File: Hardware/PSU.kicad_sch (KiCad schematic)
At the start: 20 parts, among them SW1 Power_Hard, SW2 Power_Soft, U4 TLV74115_SOT23-5, U5 TLV74133_SOT23-5

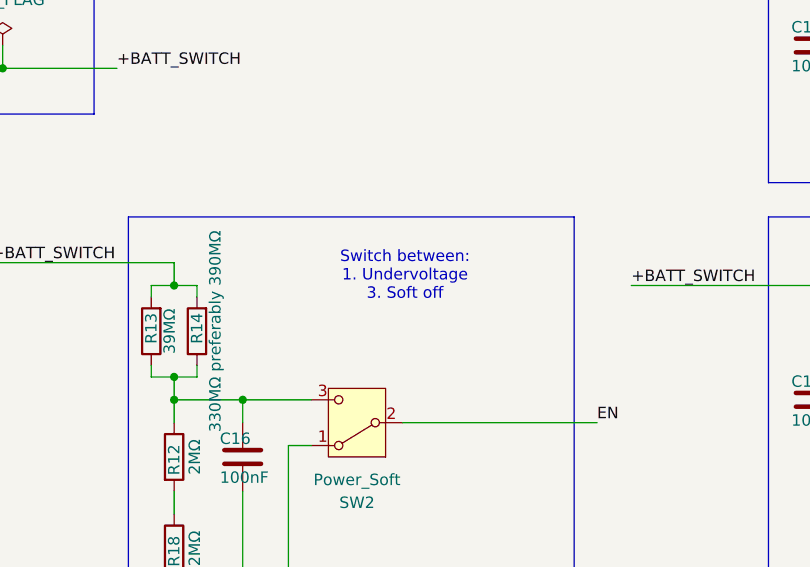
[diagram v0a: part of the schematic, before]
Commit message: Changed text PSU EN switch to match circuit
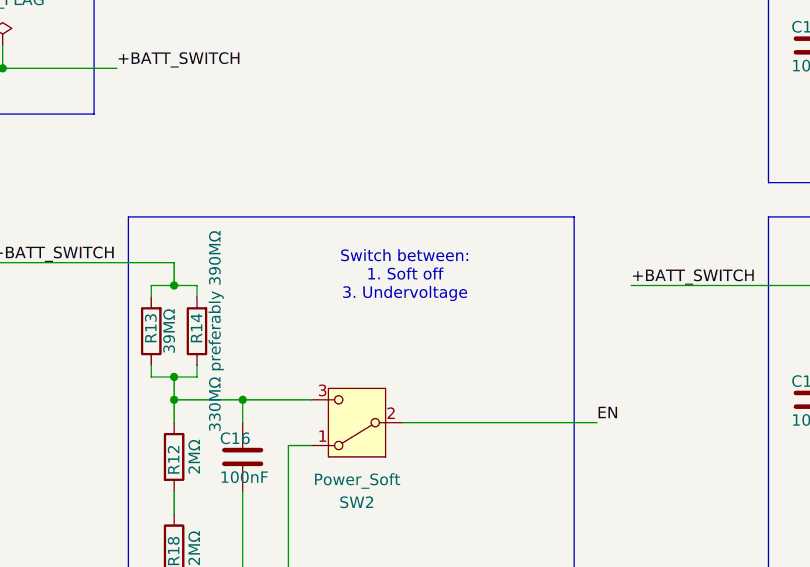
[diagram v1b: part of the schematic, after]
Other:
- note added: "Switch between: 1. Soft off 3. Undervoltage"
- note removed: "Switch between: 1. Undervoltage 3. Soft off"
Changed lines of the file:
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@@
 		)
 	)
-	(text "Switch between:\n1. Undervoltage\n3. Soft off"
+	(text "Switch between:\n1. Soft off\n3. Undervoltage"
 		(exclude_from_sim no)
 		(at 131.064 76.454 0)
